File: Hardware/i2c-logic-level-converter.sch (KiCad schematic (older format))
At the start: 8 parts, among them P1 CONN_01X04, P2 CONN_01X04, Q1 Q_NMOS_SGD, Q2 Q_NMOS_SGD

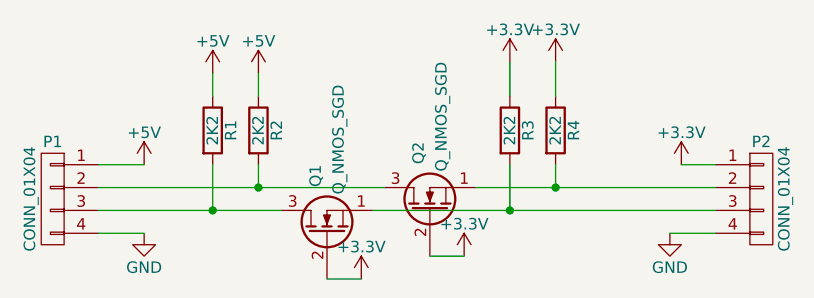
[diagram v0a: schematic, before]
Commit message: Improve documenting on schematic
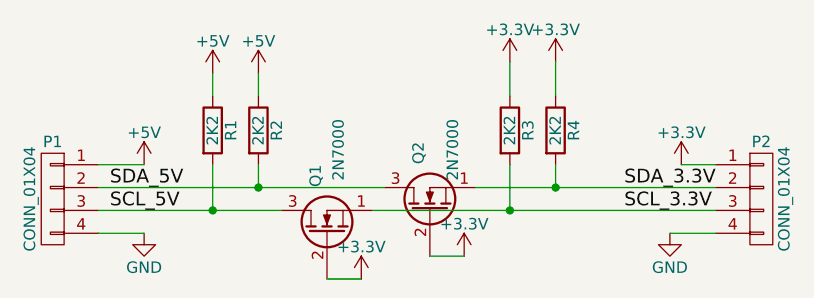
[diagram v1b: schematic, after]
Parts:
- Q1, Q2: value Q_NMOS_SGD -> 2N7000
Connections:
- net SCL_3.3V: now reaches P2.3 (P3), Q1.1 (S), R3.2
- net SCL_5V: now reaches P1.3 (P3), Q1.3 (D), R1.2
- net SDA_3.3V: now reaches P2.2 (P2), Q2.1 (S), R4.2
- net SDA_5V: now reaches P1.2 (P2), Q2.3 (D), R2.2
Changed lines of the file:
@@
 LIBS:contrib
 LIBS:valves
+LIBS:i2c-logic-level-converter-cache
 EELAYER 25 0
 EELAYER END
@@
 P 3700 1950
 F 0 "Q1" H 4000 2000 50  0000 R CNN
-F 1 "Q_NMOS_SGD" H 4350 1900 50  0000 R CNN
+F 1 "2N7000" H 4200 1900 50  0000 R CNN
 F 2 "TO_SOT_Packages_THT:TO-92_Molded_Wide_Oval" H 3900 2050 50  0001 C CNN
 F 3 "" H 3700 1950 50  0000 C CNN
@@
 P 4150 1850
 F 0 "Q2" H 4450 1900 50  0000 R CNN
-F 1 "Q_NMOS_SGD" H 4800 1800 50  0000 R CNN
+F 1 "2N7000" H 4550 1750 50  0000 R CNN
 F 2 "TO_SOT_Packages_THT:TO-92_Molded_Wide_Oval" H 4350 1950 50  0001 C CNN
 F 3 "" H 4150 1850 50  0000 C CNN
@@
 	-1   0    0    -1
 $EndComp
+Text Label 2750 1750 0    60   ~ 0
+SDA_5V
+Text Label 2750 1850 0    60   ~ 0
+SCL_5V
+Text Label 5000 1750 0    60   ~ 0
+SDA_3.3V
+Text Label 5000 1850 0    60   ~ 0
+SCL_3.3V
 $EndSCHEMATC
